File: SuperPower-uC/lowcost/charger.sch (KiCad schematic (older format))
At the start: 17 parts, among them J2 Thermistor, Q1 AO3401A, Q2 AO3401A, U3 LC709203FQH, U4 TP4056

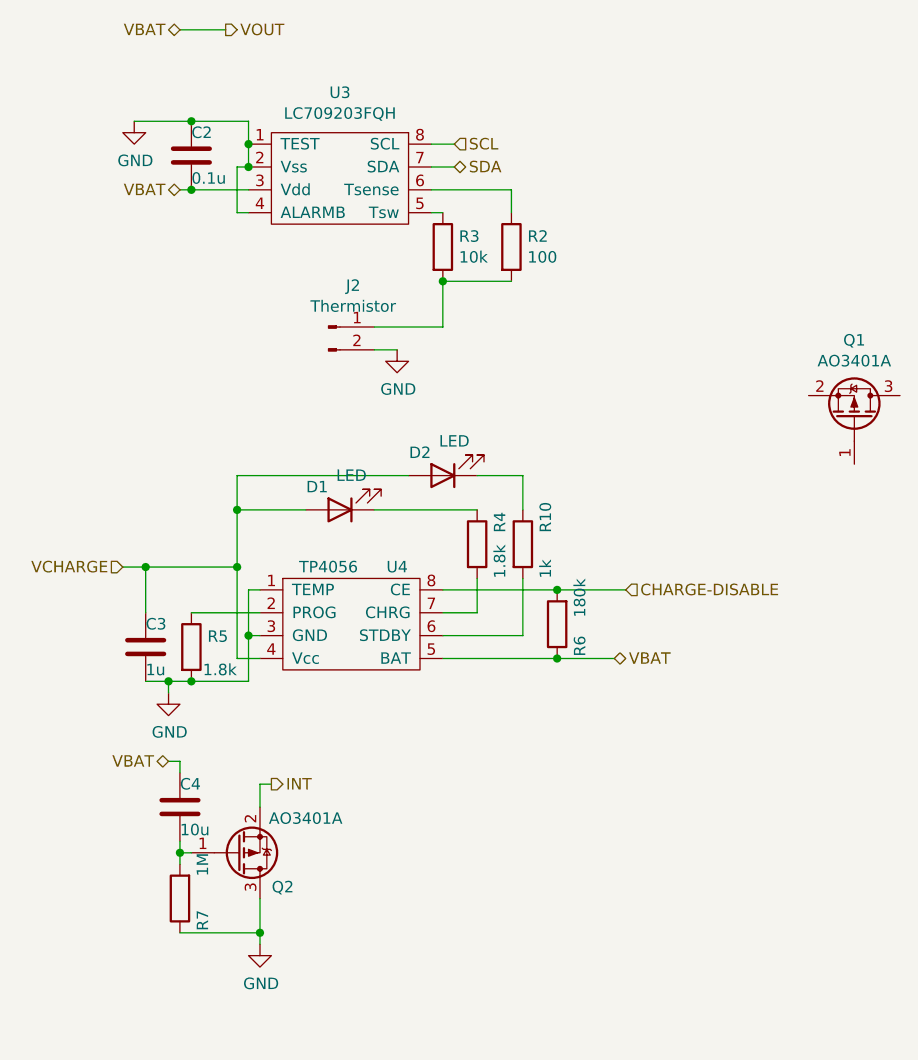
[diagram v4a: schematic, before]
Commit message: swapped p mos to n mos in for POR circuit and added toplevel components
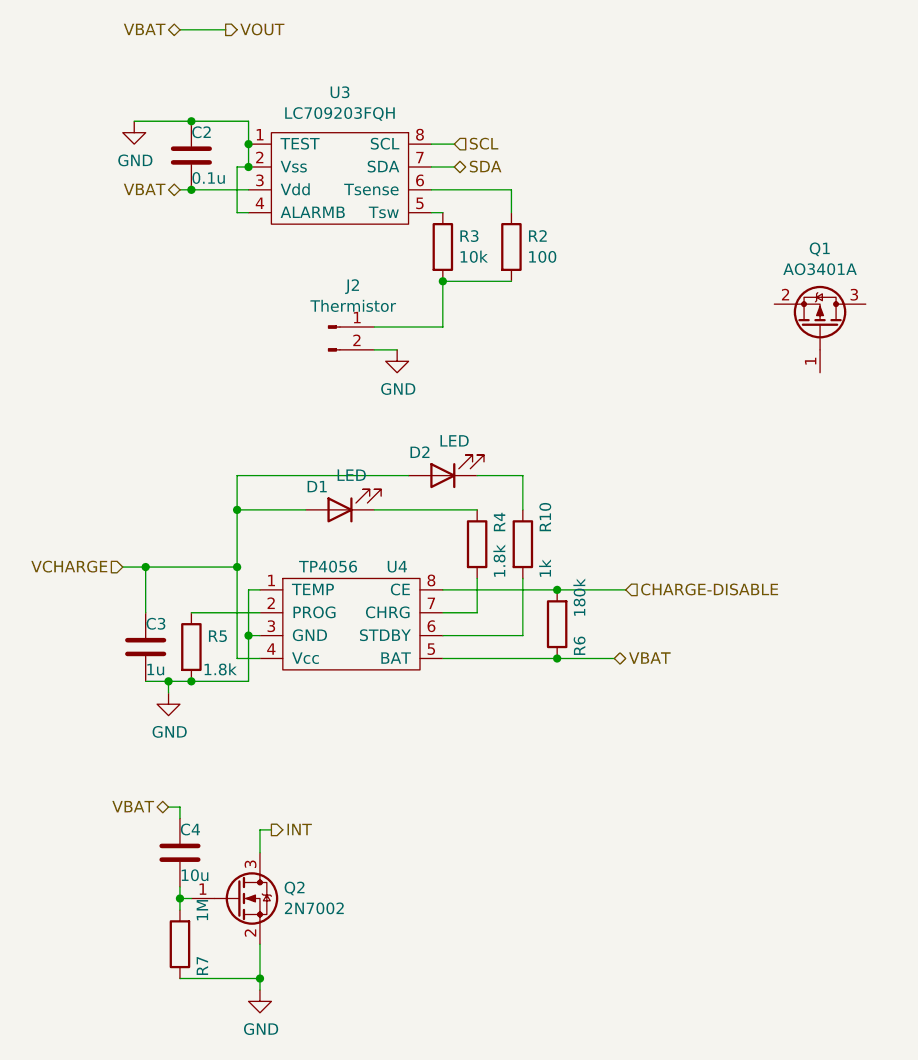
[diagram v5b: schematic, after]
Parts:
- removed Q2: AO3401A, Package_TO_SOT_SMD:SOT-23_Handsoldering, symbol Transistor_FET:AO3401A
- added Q2: 2N7002, Package_TO_SOT_SMD:SOT-23, symbol Transistor_FET:2N7002
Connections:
- net GND: now also Q2.2 (S)
- net INT: now also Q2.3 (D)
- net at C4.2, R7.2: now also Q2.1 (G)
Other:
- moved on the sheet: C4, Q1, R7
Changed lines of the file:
@@
 Text HLabel 1150 950  0    50   BiDi ~ 0
 VBAT
-Text HLabel 1550 4250 2    50   Output ~ 0
+Text HLabel 1550 4450 2    50   Output ~ 0
 INT
 Wire Wire Line
 	1150 950  1350 950
-$Comp
-L Transistor_FET:AO3401A Q2
-U 1 1 5F82C373
-P 1400 4550
-F 0 "Q2" H 1600 4700 50  0000 C CNN
-F 1 "AO3401A" H 1700 4400 50  0000 C CNN
-F 2 "Package_TO_SOT_SMD:SOT-23_Handsoldering" H 1600 4475 50  0001 L CIN
-F 3 "http://www.aosmd.com/pdfs/datasheet/AO3401A.pdf" H 1400 4550 50  0001 L CNN
-F 4 "C347476" H 1400 4550 50  0001 C CNN "LCSC"
-	1    1400 4550
-	1    0    0    1
-$EndComp
 $Comp
 L Device:R R7
 U 1 1 5F832323
-P 1150 4750
-F 0 "R7" V 1050 4800 50  0000 L CNN
-F 1 "1M" V 1050 4550 50  0000 L CNN
-F 2 "Resistor_SMD:R_0603_1608Metric_Pad1.05x0.95mm_HandSolder" V 1080 4750 50  0001 C CNN
-F 3 "~" H 1150 4750 50  0001 C CNN
-F 4 "C22935" H 1150 4750 50  0001 C CNN "LCSC"
-	1    1150 4750
+P 1150 4950
+F 0 "R7" V 1050 5000 50  0000 L CNN
+F 1 "1M" V 1050 4750 50  0000 L CNN
+F 2 "Resistor_SMD:R_0603_1608Metric_Pad1.05x0.95mm_HandSolder" V 1080 4950 50  0001 C CNN
+F 3 "~" H 1150 4950 50  0001 C CNN
+F 4 "C22935" H 1150 4950 50  0001 C CNN "LCSC"
+	1    1150 4950
 	-1   0    0    1
 $EndComp
@@
 L power:GND #PWR?
 U 1 1 5F833F9C
-P 1500 4950
-F 0 "#PWR?" H 1500 4700 50  0001 C CNN
-F 1 "GND" H 1505 4777 50  0000 C CNN
-F 2 "" H 1500 4950 50  0001 C CNN
-F 3 "" H 1500 4950 50  0001 C CNN
-	1    1500 4950
-	1    0    0    -1
-$EndComp
-Wire Wire Line
-	1150 4900 1500 4900
-Wire Wire Line
-	1500 4900 1500 4950
-Wire Wire Line
-	1500 4900 1500 4750
-Connection ~ 1500 4900
-Wire Wire Line
-	1200 4550 1150 4550
-Wire Wire Line
-	1150 4550 1150 4600
-Wire Wire Line
-	1500 4350 1500 4250
-Wire Wire Line
-	1500 4250 1550 4250
+P 1500 5150
+F 0 "#PWR?" H 1500 4900 50  0001 C CNN
+F 1 "GND" H 1505 4977 50  0000 C CNN
+F 2 "" H 1500 5150 50  0001 C CNN
+F 3 "" H 1500 5150 50  0001 C CNN
+	1    1500 5150
+	1    0    0    -1
+$EndComp
+Wire Wire Line
+	1150 5100 1500 5100
+Wire Wire Line
+	1500 5100 1500 5150
+Wire Wire Line
+	1500 5100 1500 4950
+Connection ~ 1500 5100
+Wire Wire Line
+	1200 4750 1150 4750
+Wire Wire Line
+	1150 4750 1150 4800
+Wire Wire Line
+	1500 4550 1500 4450
+Wire Wire Line
+	1500 4450 1550 4450
 $Comp
 L Device:C C4
 U 1 1 5F837984
-P 1150 4350
-F 0 "C4" H 1150 4450 50  0000 L CNN
-F 1 "10u" H 1150 4250 50  0000 L CNN
-F 2 "Capacitor_SMD:C_0603_1608Metric_Pad1.05x0.95mm_HandSolder" H 1188 4200 50  0001 C CNN
-F 3 "~" H 1150 4350 50  0001 C CNN
-F 4 "C19702" H 1150 4350 50  0001 C CNN "LCSC"
-	1    1150 4350
-	1    0    0    -1
-$EndComp
-Text HLabel 1100 4150 0    50   BiDi ~ 0
+P 1150 4550
+F 0 "C4" H 1150 4650 50  0000 L CNN
+F 1 "10u" H 1150 4450 50  0000 L CNN
+F 2 "Capacitor_SMD:C_0603_1608Metric_Pad1.05x0.95mm_HandSolder" H 1188 4400 50  0001 C CNN
+F 3 "~" H 1150 4550 50  0001 C CNN
+F 4 "C19702" H 1150 4550 50  0001 C CNN "LCSC"
+	1    1150 4550
+	1    0    0    -1
+$EndComp
+Text HLabel 1100 4350 0    50   BiDi ~ 0
 VBAT
 Wire Wire Line
-	1100 4150 1150 4150
-Wire Wire Line
-	1150 4150 1150 4200
-Wire Wire Line
-	1150 4500 1150 4550
-Connection ~ 1150 4550
+	1100 4350 1150 4350
+Wire Wire Line
+	1150 4350 1150 4400
+Wire Wire Line
+	1150 4700 1150 4750
+Connection ~ 1150 4750
 Wire Wire Line
 	1100 3800 1200 3800
@@
 L Transistor_FET:AO3401A Q1
 U 1 1 5F8021C7
-P 4100 2650
-F 0 "Q1" V 4442 2650 50  0000 C CNN
-F 1 "AO3401A" V 4351 2650 50  0000 C CNN
-F 2 "Package_TO_SOT_SMD:SOT-23_Handsoldering" H 4300 2575 50  0001 L CIN
-F 3 "http://www.aosmd.com/pdfs/datasheet/AO3401A.pdf" H 4100 2650 50  0001 L CNN
-F 4 "C347476" V 4100 2650 50  0001 C CNN "LCSC"
-	1    4100 2650
+P 3950 2250
+F 0 "Q1" V 4292 2250 50  0000 C CNN
+F 1 "AO3401A" V 4201 2250 50  0000 C CNN
+F 2 "Package_TO_SOT_SMD:SOT-23_Handsoldering" H 4150 2175 50  0001 L CIN
+F 3 "http://www.aosmd.com/pdfs/datasheet/AO3401A.pdf" H 3950 2250 50  0001 L CNN
+F 4 "C347476" V 3950 2250 50  0001 C CNN "LCSC"
+	1    3950 2250
 	0    1    -1   0
 $EndComp
@@
 Wire Wire Line
 	2800 3700 2300 3700
+$Comp
+L Transistor_FET:2N7002 Q2
+U 1 1 5F7E71FE
+P 1400 4750
+F 0 "Q2" H 1604 4796 50  0000 L CNN
+F 1 "2N7002" H 1604 4705 50  0000 L CNN
+F 2 "Package_TO_SOT_SMD:SOT-23" H 1600 4675 50  0001 L CIN
+F 3 "https://www.fairchildsemi.com/datasheets/2N/2N7002.pdf" H 1400 4750 50  0001 L CNN
+	1    1400 4750
+	1    0    0    -1
+$EndComp
 $EndSCHEMATC

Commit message: added diode to Power on Interrupt for faster recovery
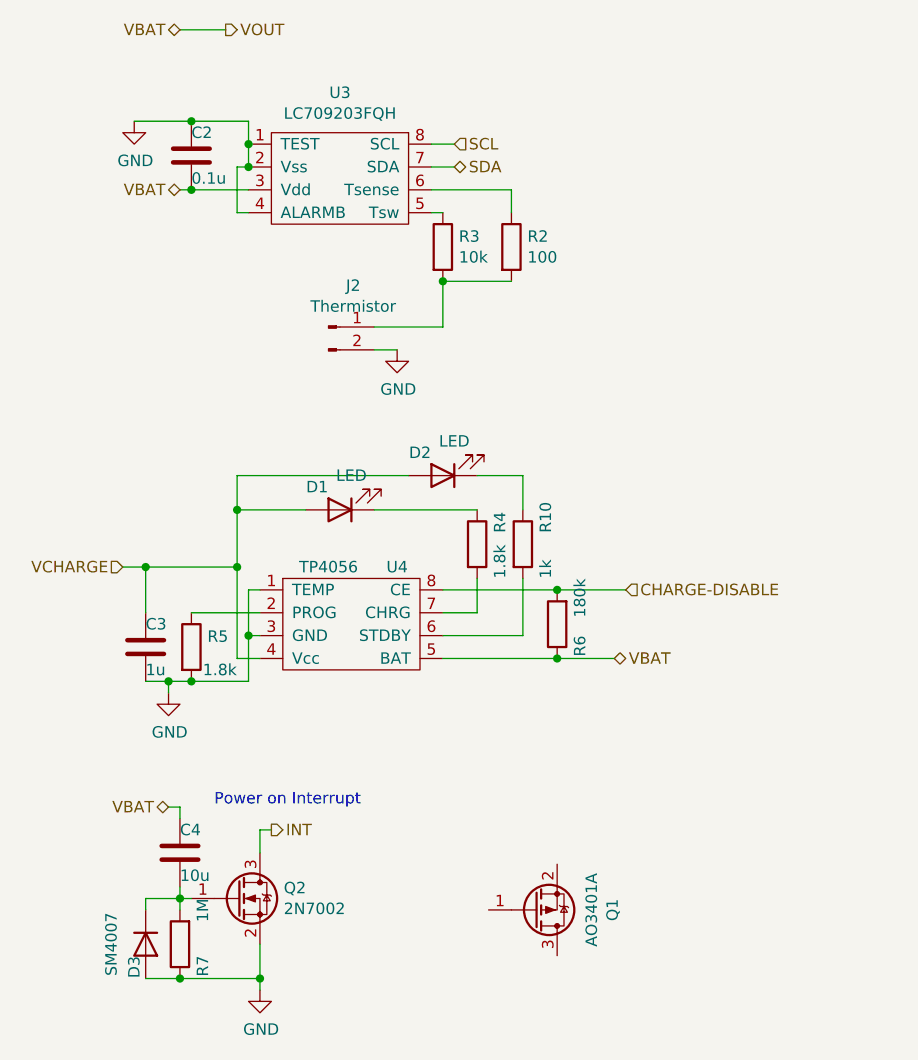
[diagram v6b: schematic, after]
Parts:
- added D3: SM4007, Diode_SMD:D_MELF, symbol Diode:SM4007
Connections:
- net GND: now also D3.2 (A)
- net at C4.2, Q2.1 (G), R7.2: now also D3.1 (K)
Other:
- note added: "Power on Interrupt"
- moved on the sheet: Q1
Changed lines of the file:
@@
 $EndComp
-Wire Wire Line
-	1150 5100 1500 5100
 Wire Wire Line
 	1500 5100 1500 5150
@@
 L Transistor_FET:AO3401A Q1
 U 1 1 5F8021C7
-P 3950 2250
-F 0 "Q1" V 4292 2250 50  0000 C CNN
-F 1 "AO3401A" V 4201 2250 50  0000 C CNN
-F 2 "Package_TO_SOT_SMD:SOT-23_Handsoldering" H 4150 2175 50  0001 L CIN
-F 3 "http://www.aosmd.com/pdfs/datasheet/AO3401A.pdf" H 3950 2250 50  0001 L CNN
-F 4 "C347476" V 3950 2250 50  0001 C CNN "LCSC"
-	1    3950 2250
-	0    1    -1   0
+P 2700 4800
+F 0 "Q1" V 3042 4800 50  0000 C CNN
+F 1 "AO3401A" V 2951 4800 50  0000 C CNN
+F 2 "Package_TO_SOT_SMD:SOT-23_Handsoldering" H 2900 4725 50  0001 L CIN
+F 3 "http://www.aosmd.com/pdfs/datasheet/AO3401A.pdf" H 2700 4800 50  0001 L CNN
+F 4 "C347476" V 2700 4800 50  0001 C CNN "LCSC"
+	1    2700 4800
+	1    0    0    1
 $EndComp
 $Comp
@@
 	1    0    0    -1
 $EndComp
+$Comp
+L Diode:SM4007 D3
+U 1 1 5F7ECCE7
+P 1000 4950
+F 0 "D3" H 1100 4900 50  0000 C CNN
+F 1 "SM4007" H 1000 4800 50  0000 C CNN
+F 2 "Diode_SMD:D_MELF" H 1000 4775 50  0001 C CNN
+F 3 "http://cdn-reichelt.de/documents/datenblatt/A400/SMD1N400%23DIO.pdf" H 1000 4950 50  0001 C CNN
+F 4 "C64898" H 1000 4950 50  0001 C CNN "LCSC"
+	1    1000 4950
+	0    1    1    0
+$EndComp
+Wire Wire Line
+	1150 4750 1000 4750
+Wire Wire Line
+	1000 4750 1000 4800
+Wire Wire Line
+	1000 5100 1150 5100
+Connection ~ 1150 5100
+Wire Wire Line
+	1150 5100 1500 5100
+Text Notes 1300 4350 0    50   ~ 0
+Power on Interrupt
 $EndSCHEMATC

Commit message: io expander, rtc cirquit, i2c pullup...
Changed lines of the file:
@@
 Comment4 ""
 $EndDescr
-Text HLabel 1350 950  2    50   Output ~ 0
-VOUT
-Text HLabel 1150 950  0    50   BiDi ~ 0
+Text HLabel 3050 3700 2    50   BiDi ~ 0
 VBAT
 Text HLabel 1550 4450 2    50   Output ~ 0
 INT
-Wire Wire Line
-	1150 950  1350 950
 $Comp
 L Device:R R7
@@
 	1    0    0    -1
 $EndComp
-Text HLabel 1100 4350 0    50   BiDi ~ 0
-VBAT
 Wire Wire Line
 	1100 4350 1150 4350
@@
 Text HLabel 3100 3400 2    50   Input ~ 0
 CHARGE-DISABLE
-Text HLabel 3050 3700 2    50   BiDi ~ 0
-VBAT
 $Comp
 L Transistor_FET:AO3401A Q1
@@
 Text Notes 1300 4350 0    50   ~ 0
 Power on Interrupt
+Text HLabel 1100 4350 0    50   BiDi ~ 0
+VBAT
 $EndSCHEMATC

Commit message: naming fixes, more components and continued schematics
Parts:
- Q2: LCSC (none) -> C8545
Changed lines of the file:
@@
 F 2 "Package_TO_SOT_SMD:SOT-23" H 1600 4675 50  0001 L CIN
 F 3 "https://www.fairchildsemi.com/datasheets/2N/2N7002.pdf" H 1400 4750 50  0001 L CNN
+F 4 "C8545" H 1400 4750 50  0001 C CNN "LCSC"
 	1    1400 4750
 	1    0    0    -1
